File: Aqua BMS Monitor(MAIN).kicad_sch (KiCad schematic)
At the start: 235 parts, among them J4 USB_C_Receptacle_USB2.0_14P, J5 SWD_01x04_Pin, Q13 NMOS, Q6 NPN, SW2 SW_Push, SW3 SW_Push, SW4 SW_Push, SW5 SW_Push, SW6 SW_Push, SW7 SW_Push, U1 BQ7695202, U2 STM32F205RETx, U3 AMS1117-3.3, U4 LM66100DCKR, U5 LM66100DCKR, U6 LM66100DCKR, U7 LM66100DCKR, U8 LMR51430XDDCR, X1 X322516MRB4SI

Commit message: Update Aqua BMS Monitor(MAIN).kicad_sch
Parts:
- removed MainBattIn2: Main lines, symbol Connector:Conn_01x02_Pin
- added J1: Conn_01x03_Pin, symbol Connector:Conn_01x03_Pin
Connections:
- net VSS: now also J1.3 (Pin_3)
- net Tx: now reaches U2.42 (PA9)
- net Tx: now also J1.1 (Pin_1)
- net Rx: now reaches U2.43 (PA10)
- net Rx: now also J1.2 (Pin_2)
- no-connect marks 37 -> 36

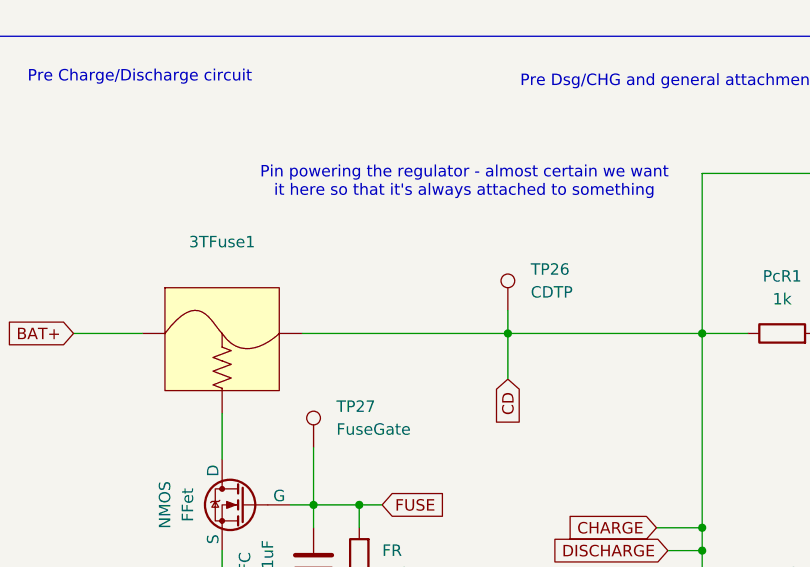
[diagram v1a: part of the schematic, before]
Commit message: Update Aqua BMS Monitor(MAIN).kicad_sch
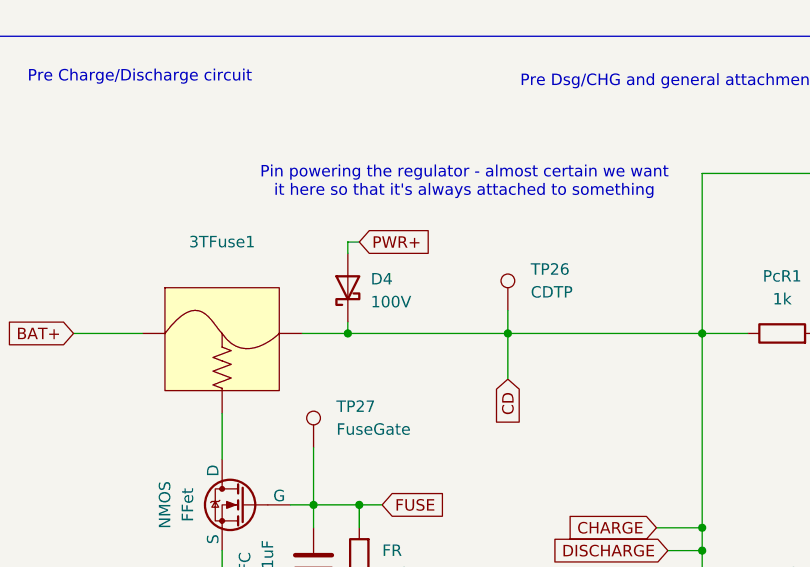
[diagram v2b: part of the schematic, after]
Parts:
- added D4: 100V, symbol Device:D_Schottky
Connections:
- net CD: now also D4.1 (K)
- net PWR+: now also D4.2 (A)
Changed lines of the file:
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@@
 	)
 	(junction
+		(at 57.15 309.88)
+		(diameter 0)
+		(color 0 0 0 0)
+	)
+	(junction
 		(at 40.64 97.79)
 		(diameter 0)
@@
 	(wire
 		(pts
+			(xy 57.15 308.61) (xy 57.15 309.88)
+		)
+		(stroke
+			(width 0)
+			(type default)
+		)
+	)
+	(wire
+		(pts
 			(xy 52.07 92.71) (xy 52.07 95.25)
 		)
@@
 	(wire
 		(pts
+			(xy 57.15 299.72) (xy 58.42 299.72)
+		)
+		(stroke
+			(width 0)
+			(type default)
+		)
+	)
+	(wire
+		(pts
 			(xy 622.3 176.53) (xy 622.3 189.23)
 		)
@@
 	(wire
 		(pts
+			(xy 57.15 309.88) (xy 74.93 309.88)
+		)
+		(stroke
+			(width 0)
+			(type default)
+		)
+	)
+	(wire
+		(pts
 			(xy 91.44 226.06) (xy 97.79 226.06)
 		)
@@
 	(wire
 		(pts
-			(xy 52.07 309.88) (xy 74.93 309.88)
+			(xy 52.07 309.88) (xy 57.15 309.88)
 		)
 		(stroke
@@
 	(wire
 		(pts
+			(xy 57.15 300.99) (xy 57.15 299.72)
+		)
+		(stroke
+			(width 0)
+			(type default)
+		)
+	)
+	(wire
+		(pts
 			(xy 81.1281 31.75) (xy 81.1281 34.29)
 		)
@@
 		)
 	)
+	(global_label "PWR+"
+		(shape input)
+		(at 58.42 299.72 0)
+		(fields_autoplaced yes)
+		(effects
+			(font
+				(size 1.27 1.27)
+			)
+			(justify left)
+		)
+		(property "Intersheetrefs" "${INTERSHEET_REFS}"
+			(at 66.969 299.72 0)
+			(hide yes)
+			(show_name no)
+			(do_not_autoplace no)
+			(effects
+				(font
+					(size 1.27 1.27)
+				)
+				(justify left)
+			)
+		)
+	)
 	(global_label "BAT-"
 		(shape input)
@@
 					(unit 1)
 				)
+			)
+		)
+	)
+	(symbol
+		(lib_id "Device:D_Schottky")
+		(at 57.15 304.8 90)
+		(unit 1)
+		(body_style 1)
+		(exclude_from_sim no)
+		(in_bom yes)
+		(on_board yes)
+		(in_pos_files yes)
+		(dnp no)
+		(fields_autoplaced yes)
+		(property "Reference" "D4"
+			(at 59.69 303.8474 90)
+			(show_name no)
+			(do_not_autoplace no)
+			(effects
+				(font
+					(size 1.27 1.27)
+				)
+				(justify right)
+			)
+		)
+		(property "Value" "100V"
+			(at 59.69 306.3874 90)
+			(show_name no)
+			(do_not_autoplace no)
+			(effects
+				(font
+					(size 1.27 1.27)
+				)
+				(justify right)
+			)
+		)
+		(property "Footprint" ""
+			(at 57.15 304.8 0)
+			(hide yes)
+			(show_name no)
+			(do_not_autoplace no)
+			(effects
+				(font
+					(size 1.27 1.27)
+				)
+			)
+		)
+		(property "Datasheet" ""
+			(at 57.15 304.8 0)
+			(hide yes)
+			(show_name no)
+			(do_not_autoplace no)
+			(effects
+				(font
+					(size 1.27 1.27)
+				)
+			)
+		)
+		(property "Description" "Schottky diode"
+			(at 57.15 304.8 0)
+			(hide yes)
+			(show_name no)
+			(do_not_autoplace no)
+			(effects
+				(font
+					(size 1.27 1.27)
+				)
+			)
+		)
+		(pin "2"
+		)
+		(pin "1"
+		)
+		(instances
+			(project "Aqua BMS Monitor(MAIN)"
+				(path "/d7eeacc8-0d33-4ea5-a0aa-fd0653295080"
+					(reference "D4")
+					(unit 1)
+				)

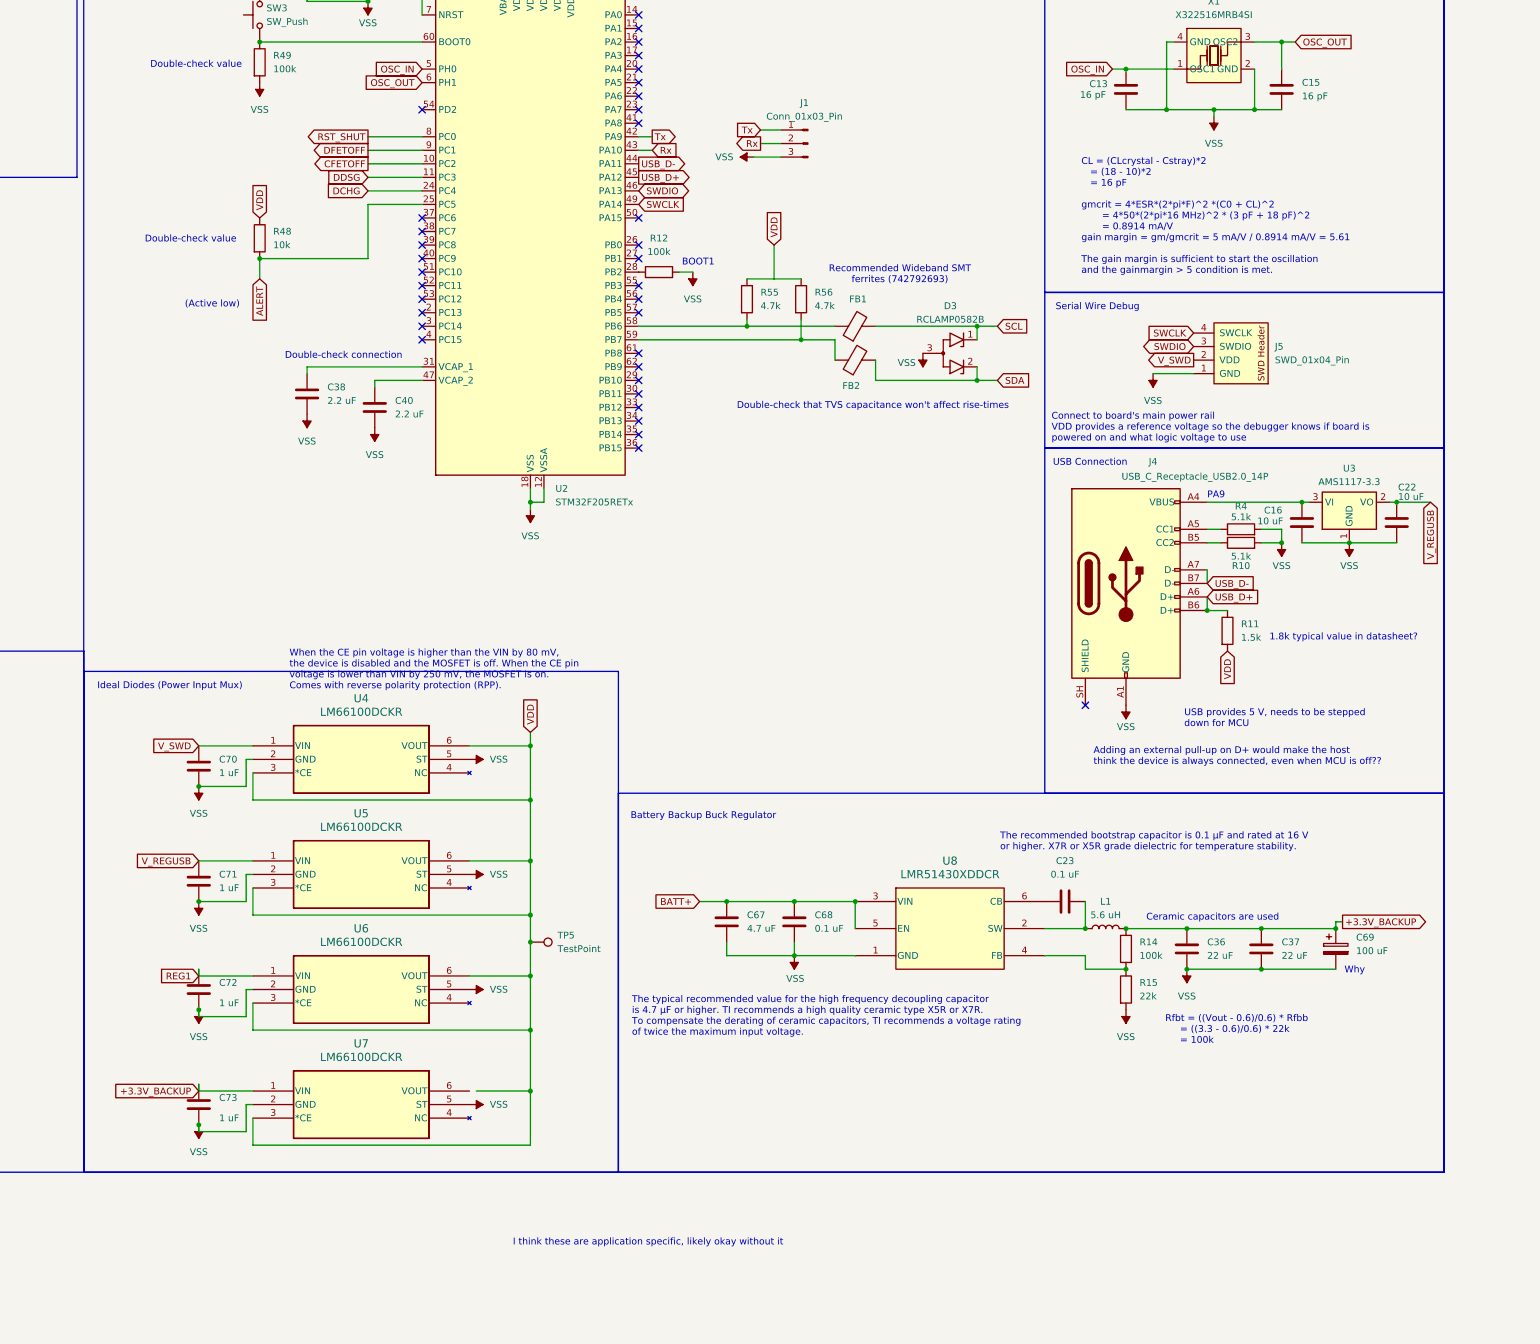
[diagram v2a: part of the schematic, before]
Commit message: Removed VR, fixed UART setup
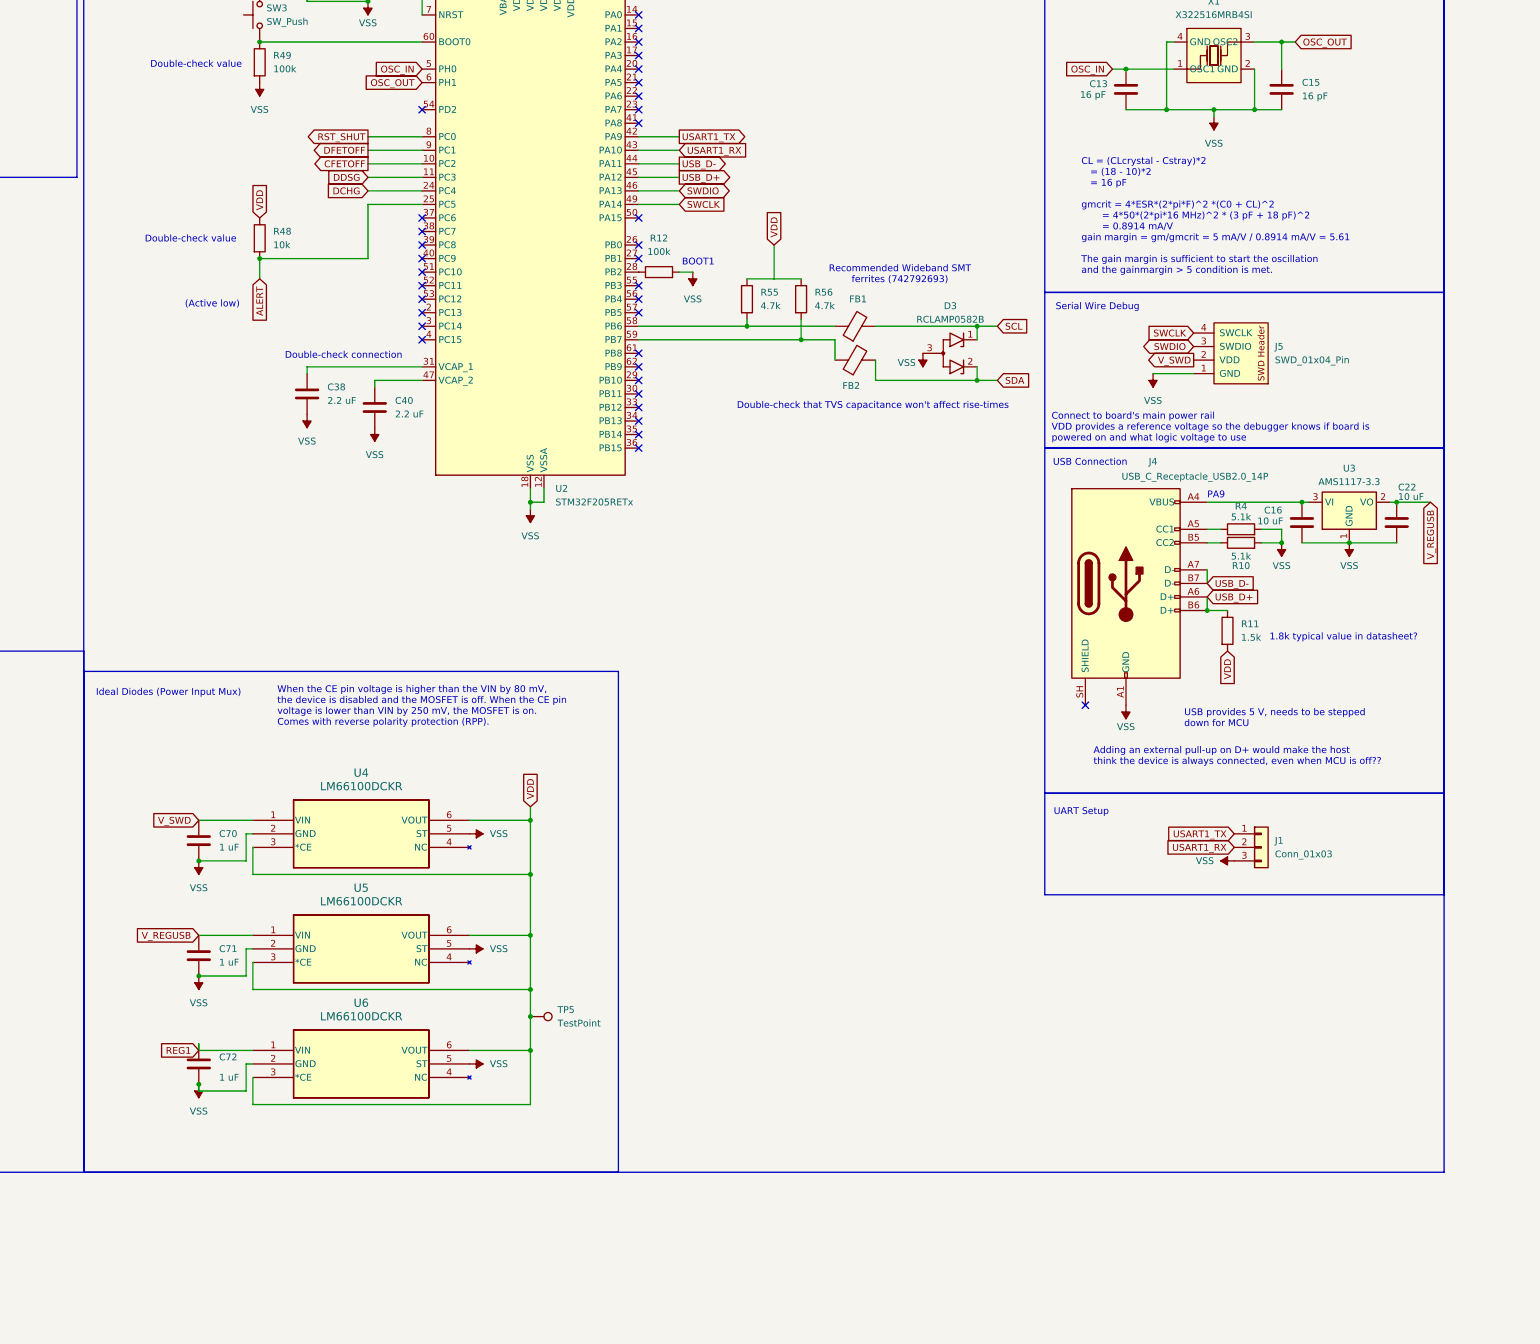
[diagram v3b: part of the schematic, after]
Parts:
- removed C23, C68: 0.1 uF, symbol Device:C
- removed C36, C37: 22 uF, symbol Device:C
- removed C67: 4.7 uF, symbol Device:C
- removed C69: 100 uF, symbol Device:C_Polarized
- removed C73: 1 uF, symbol Device:C
- removed J1: Conn_01x03_Pin, symbol Connector:Conn_01x03_Pin
- removed L1: 5.6 uH, symbol Device:L
- removed R14: 100k, symbol Device:R
- removed R15: 22k, symbol Device:R
- removed U7: LM66100DCKR, DCK6_TEX, symbol QRET_Buck_PSU-symbols:LM66100DCKR
- removed U8: LMR51430XDDCR, SOT-23-THIN-6_DDC_TEX, symbol QRET_Buck_PSU-symbols:LMR51430XDDCR
- added J1: Conn_01x03, symbol Connector_Generic:Conn_01x03
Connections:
- net VSS: now also J1.3 (Pin_3)
- net Rx renamed USART1_RX
- net USART1_RX: now also J1.2 (Pin_2)
- net Tx renamed USART1_TX
- net USART1_TX: now also J1.1 (Pin_1)
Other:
- note added: "UART Setup"
- note removed: "Battery Backup Buck Regulator"
- note removed: "Ceramic capacitors are used"
- note removed: "I think these are application specific, likely okay without it"
- note removed: "Rfbt = ((Vout - 0.6)/0.6) * Rfbb = ((3.3 - 0.6)/0.6) * 22k = 100k"
- note removed: "The recommended bootstrap capacitor is 0.1 µF and rated at 16 V or higher. X7R or X5R grade dielectric for temperature stability."
- note removed: "The typical recommended value for the high frequency decoupling capacitor is 4.7 µF or higher. TI recommends a high quality ceramic type X5R or X7R. To compensate the derating of ceramic capacitors, TI recommends a voltage rating of twice the maximum input voltage."
- note removed: "Why"
- moved on the sheet: C70, C71, C72, TP5, U4, U5, U6

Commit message: Add files via upload
Changed TVS diodes
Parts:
- removed D3: RCLAMP0582B, Package_TO_SOT_SMD:SOT-416, symbol Power_Protection:RCLAMP0582B
- added D12, D16: PTVSUC3D5VB, easyeda2kicad:SOD-323_L1.8-W1.3-LS2.5-BI, symbol 5V_TVS_BI:PTVSUC3D5VB
- C1-0, C11, C12, C13, C15, C16, C17, C18, C19, C2-0, C20, C22, C24, C27, C34, C35, C38, C39, C4, C40, C41, C42, C43, C45, C46, C47, C49, C51, C52, C53, C58, C59, C60, C61, C62, C63, C64, C65, C7, C70, C71, C72, CC2-1, CC3-2, CC4-3, ChC1, ChC2, SC1, SC2, SC3, XC1, XC2, XC3, XC4, XC5: footprint (none) -> Capacitor_SMD:C_1210_3225Metric_Pad1.33x2.70mm_HandSolder
- U4, U5, U6: footprint DCK6_TEX -> easyeda2kicad:LM66100DCKR
- XCreg1: renamed from XCreg; footprint (none) -> Capacitor_SMD:C_1210_3225Metric_Pad1.33x2.70mm_HandSolder
- XCshun1: renamed from XCshun; footprint (none) -> Capacitor_SMD:C_1210_3225Metric_Pad1.33x2.70mm_HandSolder
- renumbered ChFet to ChFet1, DBlokFet to DBlokFet1, FC to FC1, FFet to FFet1, FR to FR1, FRShunt to FRShunt1, PackR to PackR1, PcFet to PcFet1, PdFet to PdFet1, Rshunt to Rshunt1, SRinN to SRinN1, SRinP to SRinP1, TsRST to TsRST1, XRreg to XRreg1, Xout to Xout1, Xshun to Xshun1
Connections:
- net SCL: now also D12.2, D16.2
- net VSS: now also D12.1, D16.1
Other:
- note added: "No longer needed?"
- moved on the sheet: FB2

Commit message: Assigned some footprints
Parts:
- removed C17: C, Capacitor_SMD:C_1210_3225Metric_Pad1.33x2.70mm_HandSolder, symbol Device:C
- BQ296115DSGR1: footprint (none) -> easyeda2kicad:BQ296115DSGR
- C1-0, C2-0, C27, CC2-1, CC3-2, CC4-3: footprint Capacitor_SMD:C_1210_3225Metric_Pad1.33x2.70mm_HandSolder -> easyeda2kicad:220nF_C1210
- C11, C4: footprint Capacitor_SMD:C_1210_3225Metric_Pad1.33x2.70mm_HandSolder -> easyeda2kicad:100pF_C0603
- C12: footprint Capacitor_SMD:C_1210_3225Metric_Pad1.33x2.70mm_HandSolder -> easyeda2kicad:0.47 uF_C1210
- C13, C15: footprint Capacitor_SMD:C_1210_3225Metric_Pad1.33x2.70mm_HandSolder -> easyeda2kicad:16pF_C0805
- C16, C22: footprint Capacitor_SMD:C_1210_3225Metric_Pad1.33x2.70mm_HandSolder -> easyeda2kicad:10uF_C1210
- C18, C19, C24, C65, C70, C71, C72: footprint Capacitor_SMD:C_1210_3225Metric_Pad1.33x2.70mm_HandSolder -> easyeda2kicad:1uF_C1210
- C20: footprint Capacitor_SMD:C_1210_3225Metric_Pad1.33x2.70mm_HandSolder -> easyeda2kicad:22nF_C1210
- C34, C35, C39, C41, C42, C43, C45, C46, C47, C49, C51, C52, C53, C58, C59, C60, C61, C62, C63, ChC1, ChC2: footprint Capacitor_SMD:C_1210_3225Metric_Pad1.33x2.70mm_HandSolder -> easyeda2kicad:0.1uF_C1210
- C38, C40: footprint Capacitor_SMD:C_1210_3225Metric_Pad1.33x2.70mm_HandSolder -> easyeda2kicad:2.2uF_C1210
- C64: footprint Capacitor_SMD:C_1210_3225Metric_Pad1.33x2.70mm_HandSolder -> easyeda2kicad:4.7uF_C1210
- C7: footprint Capacitor_SMD:C_1210_3225Metric_Pad1.33x2.70mm_HandSolder -> easyeda2kicad:1nF_C0805
- CR1, CR2, CR3, CR4, CR5: footprint (none) -> easyeda2kicad:50_R0603
- ChD1, D1, D13, D15, D2, D4, D8, D9: footprint (none) -> easyeda2kicad:100V_Schottky
- ChD2, D14, D17: footprint (none) -> easyeda2kicad:16V_Zener
- ChFet1, DBlokFet1, DBlokFet2, DFet2, Dfet1, FFet1, Q13: footprint (none) -> easyeda2kicad:NMOS
- ChR1, PcR2, PdR2, R22, R43, R46: footprint (none) -> easyeda2kicad:10M_R1210
- ChR2, PcR3, PdR3, R10, R32, R4, R42: footprint (none) -> easyeda2kicad:5.1k_R1210
- D12, D16: footprint easyeda2kicad:SOD-323_L1.8-W1.3-LS2.5-BI -> easyeda2kicad:5V_TVS_SOD-323_L1.8-W1.3-LS2.5-BI
- DRgate1, R41, R63, R64: footprint (none) -> easyeda2kicad:51_R1206
- FB1, FB2: footprint (none) -> easyeda2kicad:2.2k_Ferrite_Bead_L0603
- FC1, PCc2, PcC1, PdC1, PdC2: footprint (none) -> easyeda2kicad:0.1uF_C1210
- FR1: footprint (none) -> easyeda2kicad:20k_R1206
- FRShunt1: footprint (none) -> easyeda2kicad:1m_Shunt_4W
- J1: footprint (none) -> easyeda2kicad:3P_Pin_Header
- PackR1, R13, R35, R47, R48, TsR1: footprint (none) -> easyeda2kicad:10k_R1206
- PcFet1, PdFet1: footprint (none) -> easyeda2kicad:PMOS
- PcR1, PdR1, R36, R44, XRC1, XRC2, XRC3, XRC4, Xout1: footprint (none) -> easyeda2kicad:1k_R1206
- Q6: footprint (none) -> easyeda2kicad:NPN_BJT
- R11: footprint (none) -> easyeda2kicad:1.5k_R1210
- R12, R49: footprint (none) -> easyeda2kicad:100k_R1210
- R23: footprint (none) -> easyeda2kicad:300_R0805
- R37, R38, R65, R66: footprint (none) -> easyeda2kicad:4k_R0805
- R55, R56: footprint (none) -> easyeda2kicad:4.7k_R1210
- R6, SRinN1, SRinP1, XRC5, Xshun1: footprint (none) -> easyeda2kicad:100_R1210
- Rshunt1, Rshunt2, Rshunt3, Rshunt4: footprint (none) -> easyeda2kicad:200_R1210
- SW2, SW3, SW4, SW5, SW6, SW7, TsRST1: footprint (none) -> easyeda2kicad:SW_Push_YZA-009
- TH1, TH2, TH3: footprint (none) -> easyeda2kicad:PTC_Thermistor_TMP6131LPGM
- TsC1: footprint (none) -> easyeda2kicad:470pF_C0805
- U1: footprint BQ76952PFBR:QFP50P900X900X120-48N -> easyeda2kicad:BQ7695202PFBR
- X1: footprint easyeda2kicad:CRYSTAL-SMD_4P-L3.2-W2.5-BL-2 -> easyeda2kicad:18pF_Oscillator_CRYSTAL-SMD_4P
- XRreg1: footprint (none) -> easyeda2kicad:5_RES-SMD_L6.4-W3.8
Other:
- note added: "CL = (CLcrystal - Cstray)*2 = (18 - 10)*2 = 16 pF gmcrit = 4*ESR*(2*pi*F)^2 *(C0 + CL)^2 = 4*50*(2*pi*16 MHz)^2 * (3 pF + 16 pF)^2 = 0.729 mA/V gain margin = gm/gmcrit = 5 mA/V / 0.729 mA/V = 6.86 The gain margin is sufficient to start the oscillation and the gainmargin > 5 condition is met."
- note removed: "CL = (CLcrystal - Cstray)*2 = (18 - 10)*2 = 16 pF gmcrit = 4*ESR*(2*pi*F)^2 *(C0 + CL)^2 = 4*50*(2*pi*16 MHz)^2 * (3 pF + 18 pF)^2 = 0.8914 mA/V gain margin = gm/gmcrit = 5 mA/V / 0.8914 mA/V = 5.61 The gain margin is sufficient to start the oscillation and the gainmargin > 5 condition is met."
